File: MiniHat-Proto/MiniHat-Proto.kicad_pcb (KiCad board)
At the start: 2 copper layers, 20 x 20 mm, 2 parts, among them J101 Interface

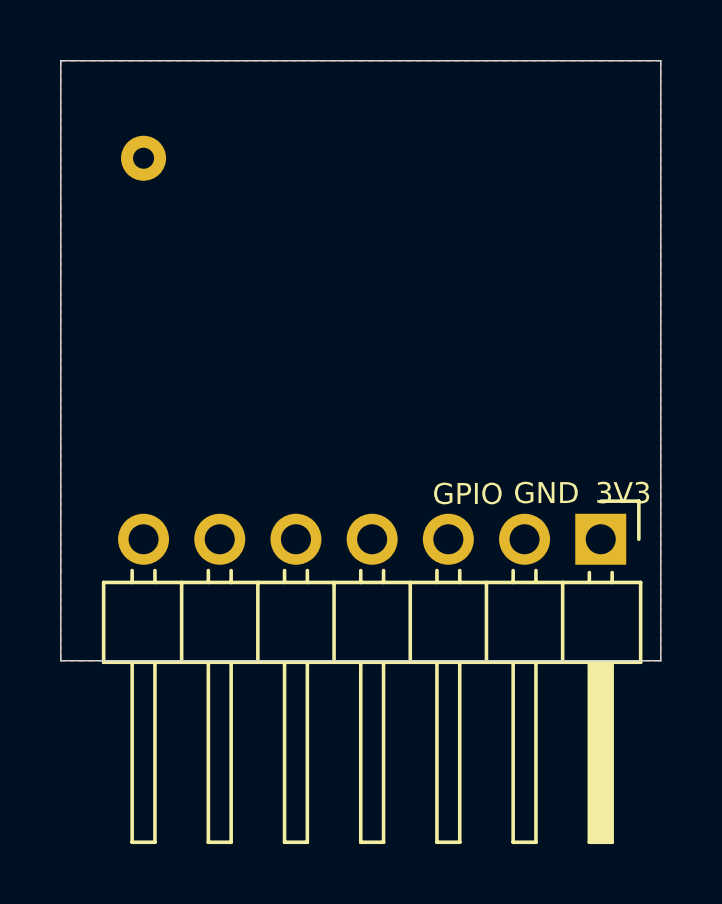
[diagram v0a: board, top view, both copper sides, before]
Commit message: New GND Pin.  Added PI Filters to all inputs.    Refined Layout
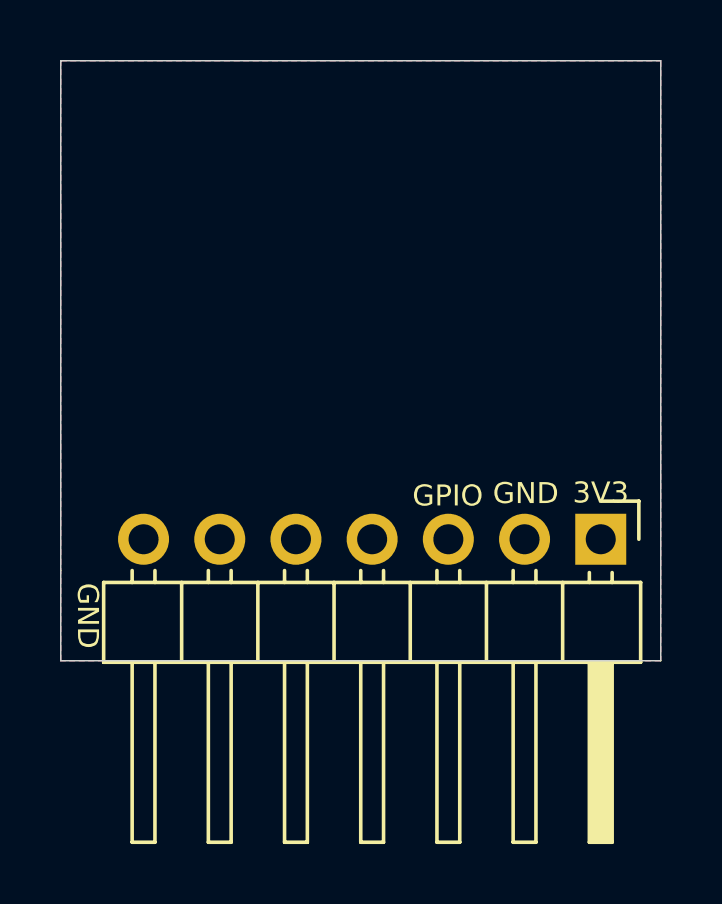
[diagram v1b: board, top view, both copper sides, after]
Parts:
- removed REF**: TestPoint_THTPad_D1.5mm_Drill0.7mm, TestPoint:TestPoint_THTPad_D1.5mm_Drill0.7mm
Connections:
- J101 pad 7: (no net) -> GND
